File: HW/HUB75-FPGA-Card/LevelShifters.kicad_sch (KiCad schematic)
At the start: 18 parts, among them J11 Conn_01x01, J12 Conn_01x01, J13 Conn_01x01, J14 Conn_01x01, J15 Conn_01x01, J16 Conn_01x01, J2 Conn_01x03, J3 Conn_02x08_Odd_Even, J4 Conn_01x03, J5 Conn_01x03, J6 Conn_02x08_Odd_Even, J7 Conn_01x03, U4 74AHCT245PW, U5 74AHCT245PW, U6 74AHCT245PW

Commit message: saving hardware progress
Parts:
- removed J13, J14, J15, J16: Conn_01x01, Connector_Wire:SolderWirePad_1x01_SMD_1x2mm, symbol Connector_Generic:Conn_01x01
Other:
- note removed: "Aux 5V Pads"
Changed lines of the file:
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@@
-    (effects (font (size 2.54 2.54)) (justify left bottom))
-  )
-  (text "Aux 5V\nPads" (at 255.27 116.84 0)
     (effects (font (size 2.54 2.54)) (justify left bottom))
   )
@@
         (path "/12c1dc17-a9d4-409d-a42e-fc131eeff0fd/eacbd1af-1c38-4bd8-912b-ae623186866b"
           (reference "#PWR048") (unit 1)
-        )
-      )
-    )
-  )
-  (symbol (lib_id "power:+5V") (at 250.19 121.92 0) (unit 1)
-    (in_bom yes) (on_board yes) (dnp no) (fields_autoplaced)
-    (property "Reference" "#PWR0102" (at 250.19 125.73 0)
-      (effects (font (size 1.27 1.27)) hide)
-    )
-    (property "Value" "+5V" (at 250.19 116.84 0)
-      (effects (font (size 1.27 1.27)))
-    )
-    (property "Footprint" "" (at 250.19 121.92 0)
-      (effects (font (size 1.27 1.27)) hide)
-    )
-    (property "Datasheet" "" (at 250.19 121.92 0)
-      (effects (font (size 1.27 1.27)) hide)
-    )
-    (pin "1")
-    (instances
-      (project "HUB75-FPGA-Card"
-        (path "/12c1dc17-a9d4-409d-a42e-fc131eeff0fd/eacbd1af-1c38-4bd8-912b-ae623186866b"
-          (reference "#PWR0102") (unit 1)
         )
       )
@@
         (path "/12c1dc17-a9d4-409d-a42e-fc131eeff0fd/eacbd1af-1c38-4bd8-912b-ae623186866b"
           (reference "J3") (unit 1)
-        )
-      )
-    )
-  )
-  (symbol (lib_id "Connector_Generic:Conn_01x01") (at 255.27 140.97 0) (unit 1)
-    (in_bom yes) (on_board yes) (dnp no) (fields_autoplaced)
-    (property "Reference" "J15" (at 257.81 139.7 0)
-      (effects (font (size 1.27 1.27)) (justify left))
-    )
-    (property "Value" "Conn_01x01" (at 257.81 142.24 0)
-      (effects (font (size 1.27 1.27)) (justify left))
-    )
-    (property "Footprint" "Connector_Wire:SolderWirePad_1x01_SMD_1x2mm" (at 255.27 140.97 0)
-      (effects (font (size 1.27 1.27)) hide)
-    )
-    (property "Datasheet" "~" (at 255.27 140.97 0)
-      (effects (font (size 1.27 1.27)) hide)
-    )
-    (pin "1")
-    (instances
-      (project "HUB75-FPGA-Card"
-        (path "/12c1dc17-a9d4-409d-a42e-fc131eeff0fd/eacbd1af-1c38-4bd8-912b-ae623186866b"
-          (reference "J15") (unit 1)
         )
       )
@@
     )
   )
-  (symbol (lib_id "power:GND") (at 250.19 127 0) (unit 1)
-    (in_bom yes) (on_board yes) (dnp no)
-    (property "Reference" "#PWR0103" (at 250.19 133.35 0)
-      (effects (font (size 1.27 1.27)) hide)
-    )
-    (property "Value" "GND" (at 250.19 130.81 0)
-      (effects (font (size 1.27 1.27)))
-    )
-    (property "Footprint" "" (at 250.19 127 0)
-      (effects (font (size 1.27 1.27)) hide)
-    )
-    (property "Datasheet" "" (at 250.19 127 0)
-      (effects (font (size 1.27 1.27)) hide)
-    )
-    (pin "1")
-    (instances
-      (project "HUB75-FPGA-Card"
-        (path "/12c1dc17-a9d4-409d-a42e-fc131eeff0fd/eacbd1af-1c38-4bd8-912b-ae623186866b"
-          (reference "#PWR0103") (unit 1)
-        )
-      )
-    )
-  )
   (symbol (lib_id "power:GND") (at 106.68 128.27 0) (unit 1)
     (in_bom yes) (on_board yes) (dnp no)
@@
     )
   )
-  (symbol (lib_id "Connector_Generic:Conn_01x01") (at 255.27 146.05 0) (unit 1)
-    (in_bom yes) (on_board yes) (dnp no) (fields_autoplaced)
-    (property "Reference" "J16" (at 257.81 144.78 0)
-      (effects (font (size 1.27 1.27)) (justify left))
-    )
-    (property "Value" "Conn_01x01" (at 257.81 147.32 0)
-      (effects (font (size 1.27 1.27)) (justify left))
-    )
-    (property "Footprint" "Connector_Wire:SolderWirePad_1x01_SMD_1x2mm" (at 255.27 146.05 0)
-      (effects (font (size 1.27 1.27)) hide)
-    )
-    (property "Datasheet" "~" (at 255.27 146.05 0)
-      (effects (font (size 1.27 1.27)) hide)
-    )
-    (pin "1")
-    (instances
-      (project "HUB75-FPGA-Card"
-        (path "/12c1dc17-a9d4-409d-a42e-fc131eeff0fd/eacbd1af-1c38-4bd8-912b-ae623186866b"
-          (reference "J16") (unit 1)
-        )
-      )
-    )
-  )
   (symbol (lib_id "power:+5V") (at 195.58 91.44 0) (unit 1)
     (in_bom yes) (on_board yes) (dnp no) (fields_autoplaced)
@@
         (path "/12c1dc17-a9d4-409d-a42e-fc131eeff0fd/eacbd1af-1c38-4bd8-912b-ae623186866b"
           (reference "J12") (unit 1)
-        )
-      )
-    )
-  )
-  (symbol (lib_id "Connector_Generic:Conn_01x01") (at 255.27 121.92 0) (unit 1)
-    (in_bom yes) (on_board yes) (dnp no) (fields_autoplaced)
-    (property "Reference" "J13" (at 257.81 120.65 0)
-      (effects (font (size 1.27 1.27)) (justify left))
-    )
-    (property "Value" "Conn_01x01" (at 257.81 123.19 0)
-      (effects (font (size 1.27 1.27)) (justify left))
-    )
-    (property "Footprint" "Connector_Wire:SolderWirePad_1x01_SMD_1x2mm" (at 255.27 121.92 0)
-      (effects (font (size 1.27 1.27)) hide)
-    )
-    (property "Datasheet" "~" (at 255.27 121.92 0)
-      (effects (font (size 1.27 1.27)) hide)
-    )
-    (pin "1")
-    (instances
-      (project "HUB75-FPGA-Card"
-        (path "/12c1dc17-a9d4-409d-a42e-fc131eeff0fd/eacbd1af-1c38-4bd8-912b-ae623186866b"
-          (reference "J13") (unit 1)
-        )
-      )
-    )
-  )
-  (symbol (lib_id "Connector_Generic:Conn_01x01") (at 255.27 127 0) (unit 1)
-    (in_bom yes) (on_board yes) (dnp no) (fields_autoplaced)
-    (property "Reference" "J14" (at 257.81 125.73 0)
-      (effects (font (size 1.27 1.27)) (justify left))
-    )
-    (property "Value" "Conn_01x01" (at 257.81 128.27 0)
-      (effects (font (size 1.27 1.27)) (justify left))
-    )
-    (property "Footprint" "Connector_Wire:SolderWirePad_1x01_SMD_1x2mm" (at 255.27 127 0)
-      (effects (font (size 1.27 1.27)) hide)
-    )
-    (property "Datasheet" "~" (at 255.27 127 0)
-      (effects (font (size 1.27 1.27)) hide)
-    )
-    (pin "1")
-    (instances
-      (project "HUB75-FPGA-Card"
-        (path "/12c1dc17-a9d4-409d-a42e-fc131eeff0fd/eacbd1af-1c38-4bd8-912b-ae623186866b"
-          (reference "J14") (unit 1)
         )
       )
@@
     )
   )
-  (symbol (lib_id "power:+5V") (at 250.19 140.97 0) (unit 1)
-    (in_bom yes) (on_board yes) (dnp no) (fields_autoplaced)
-    (property "Reference" "#PWR0104" (at 250.19 144.78 0)
-      (effects (font (size 1.27 1.27)) hide)
-    )
-    (property "Value" "+5V" (at 250.19 135.89 0)
-      (effects (font (size 1.27 1.27)))
-    )
-    (property "Footprint" "" (at 250.19 140.97 0)
-      (effects (font (size 1.27 1.27)) hide)
-    )
-    (property "Datasheet" "" (at 250.19 140.97 0)
-      (effects (font (size 1.27 1.27)) hide)
-    )
-    (pin "1")
-    (instances
-      (project "HUB75-FPGA-Card"
-        (path "/12c1dc17-a9d4-409d-a42e-fc131eeff0fd/eacbd1af-1c38-4bd8-912b-ae623186866b"
-          (reference "#PWR0104") (unit 1)
-        )
-      )
-    )
-  )
   (symbol (lib_id "power:GND") (at 182.88 57.15 0) (unit 1)
     (in_bom yes) (on_board yes) (dnp no)
@@
         )
       )
-    )
-  )
-  (symbol (lib_id "power:GND") (at 250.19 146.05 0) (unit 1)
-    (in_bom yes) (on_board yes) (dnp no)
-    (property "Reference" "#PWR0105" (at 250.19 152.4 0)
-      (effects (font (size 1.27 1.27)) hide)
-    )
-    (property "Value" "GND" (at 250.19 149.86 0)
-      (effects (font (size 1.27 1.27)))
-    )
-    (property "Footprint" "" (at 250.19 146.05 0)
-      (effects (font (size 1.27 1.27)) hide)
-    )
-    (property "Datasheet" "" (at 250.19 146.05 0)
-      (effects (font (size 1.27 1.27)) hide)
-    )
-    (pin "1")
-    (instances
-      (project "HUB75-FPGA-Card"
-        (path "/12c1dc17-a9d4-409d-a42e-fc131eeff0fd/eacbd1af-1c38-4bd8-912b-ae623186866b"
-          (reference "#PWR0105") (unit 1)
-        )
-      )

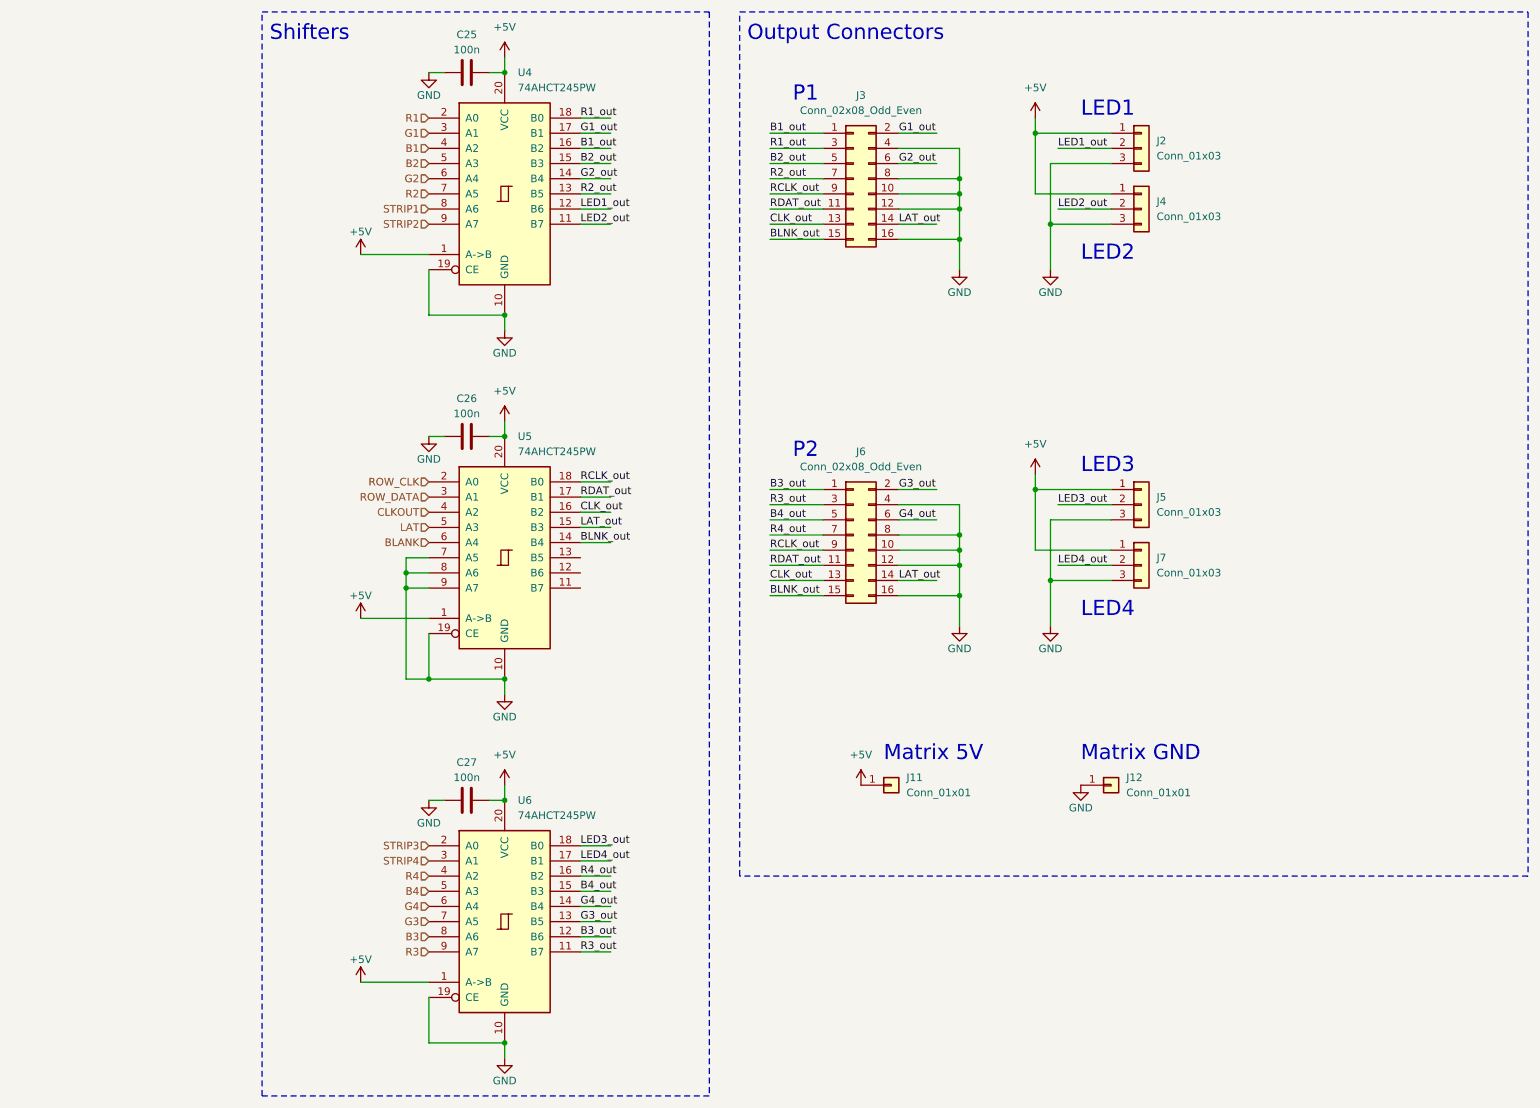
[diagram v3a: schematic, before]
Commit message: initial v1.1 board layout
still needs rp2040 pins routed
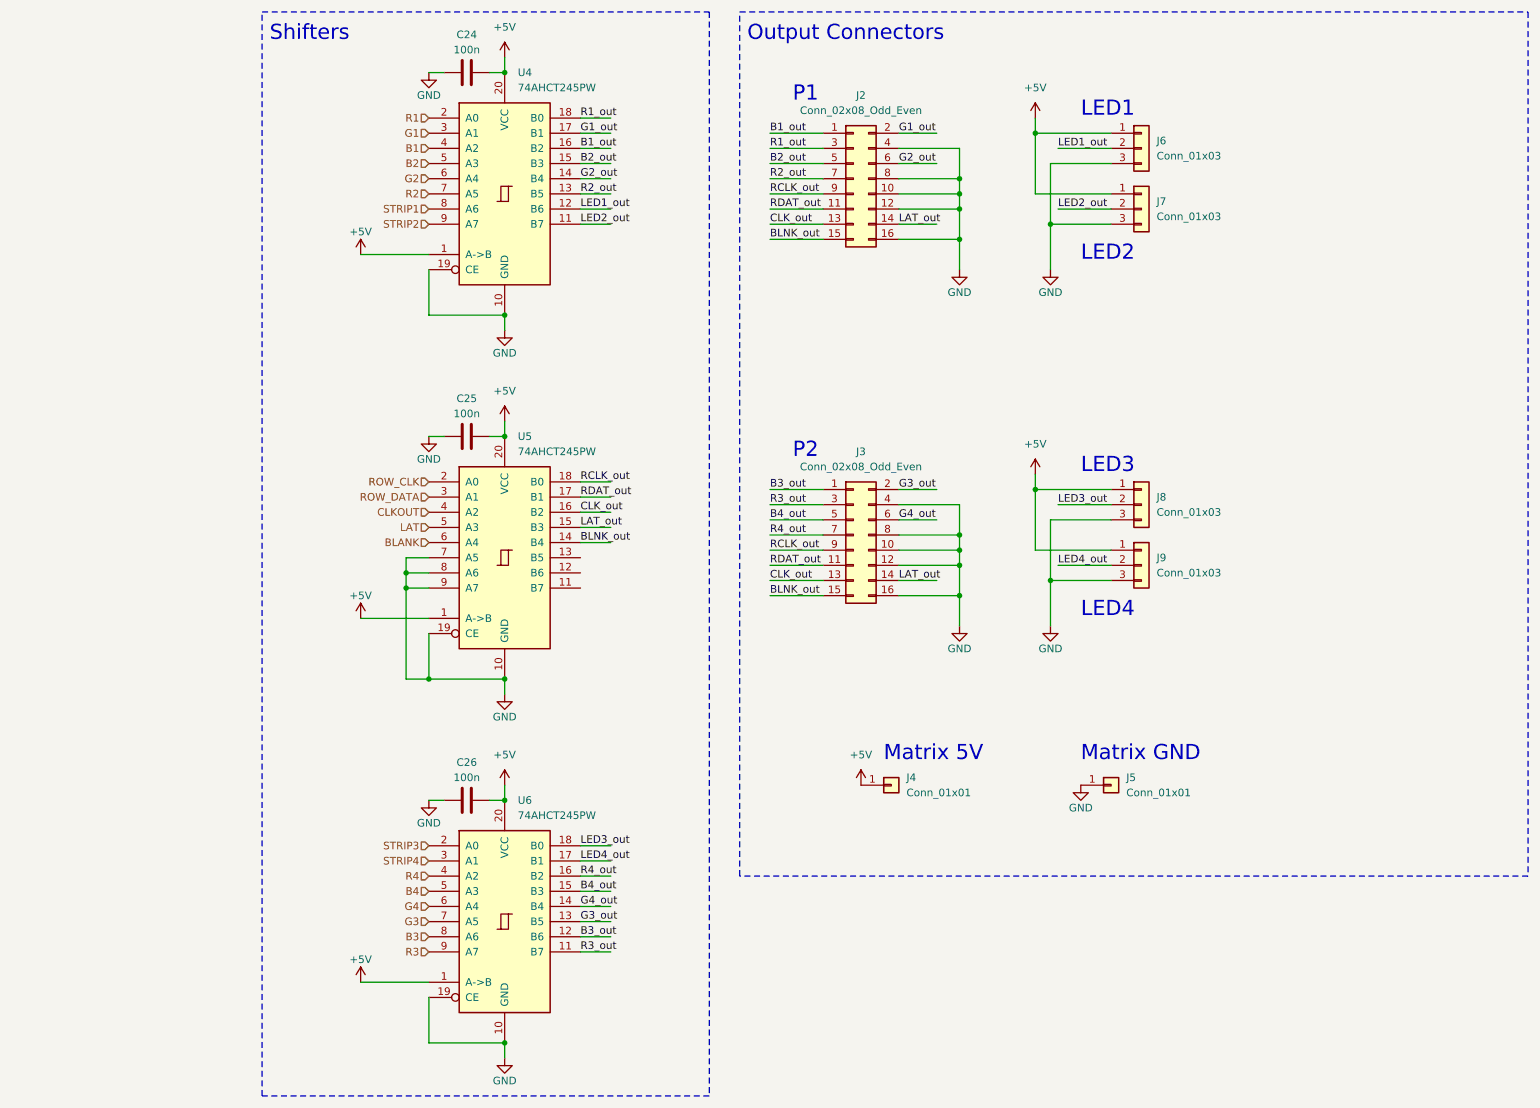
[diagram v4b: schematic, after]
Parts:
- renumbered C25 to C24, C26 to C25, C27 to C26, J3 to J2, J6 to J3, J11 to J4, J12 to J5, J2 to J6, J4 to J7, J5 to J8, J7 to J9

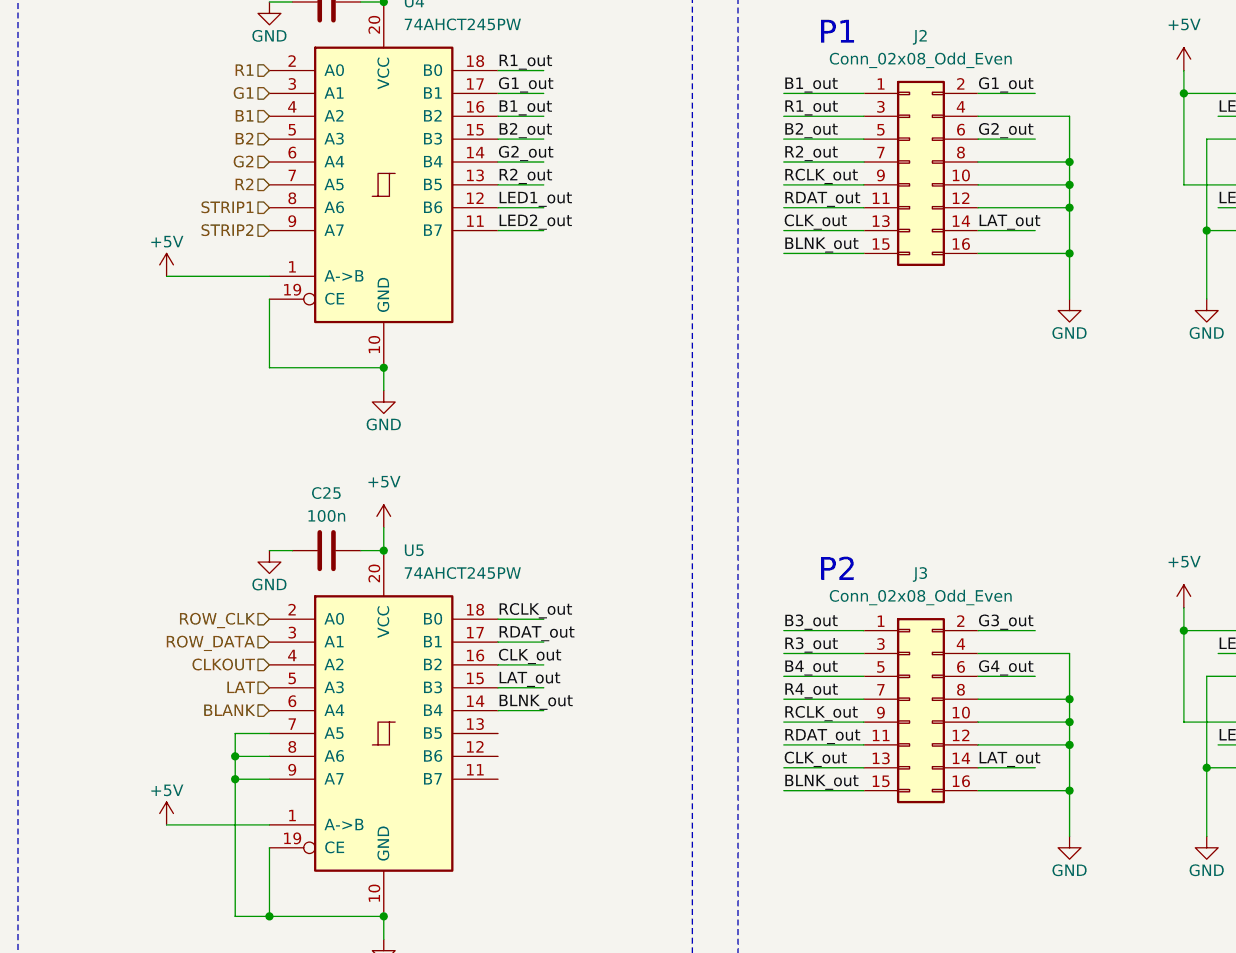
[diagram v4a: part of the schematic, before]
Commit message: update components and generate production files
still need to look into CBSEL
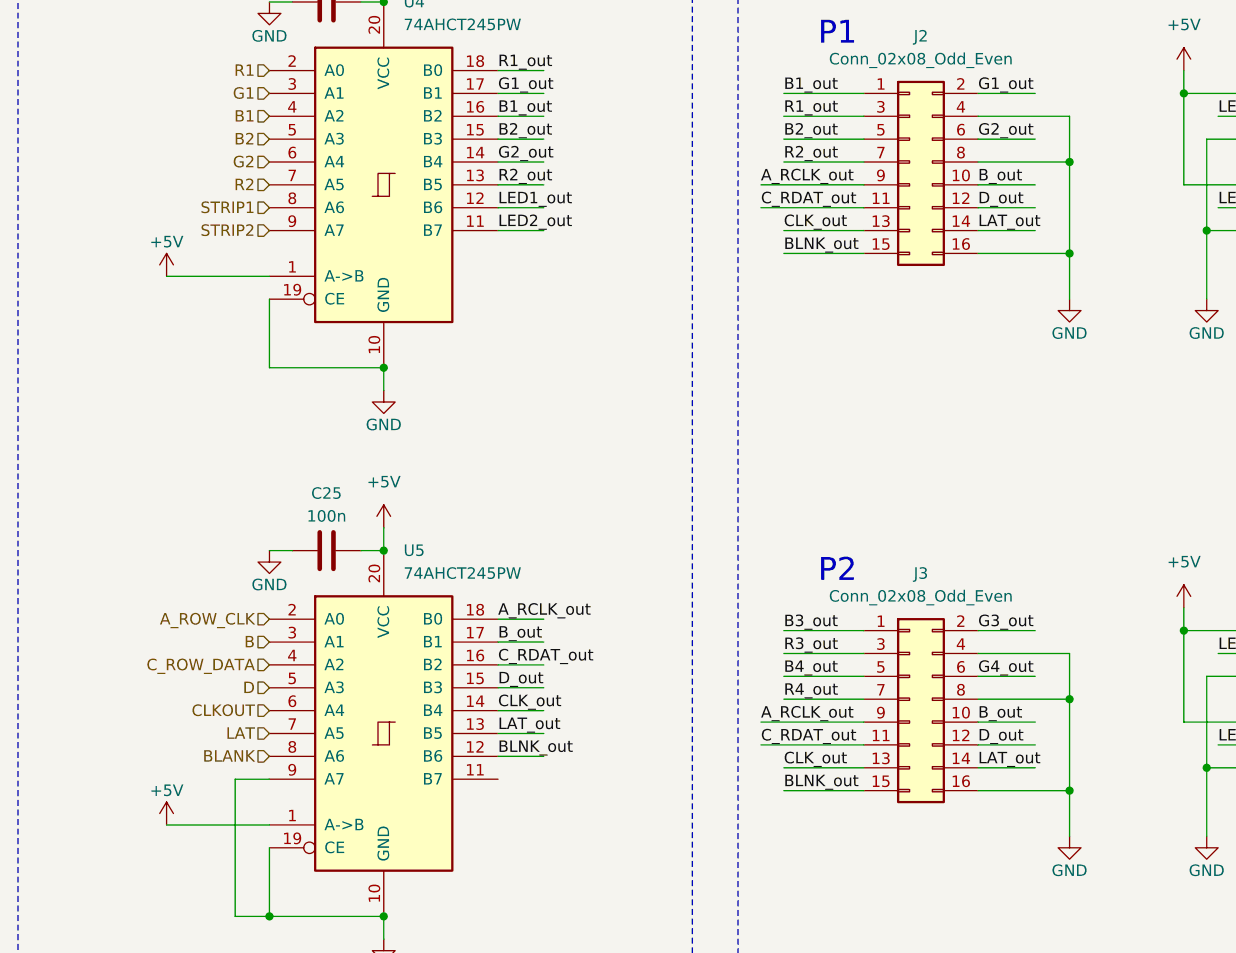
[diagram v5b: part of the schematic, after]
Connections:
- net BLANK: now also U5.8 (A6); no longer U5.6 (A4)
- net BLNK_out: now also U5.12 (B6); no longer U5.14 (B4)
- net CLKOUT: now also U5.6 (A4); no longer U5.4 (A2)
- net CLK_out: now also U5.14 (B4); no longer U5.16 (B2)
- net GND: no longer J2.10 (Pin_10), J2.12 (Pin_12), J3.10 (Pin_10), J3.12 (Pin_12), U5.7 (A5), U5.8 (A6)
- net LAT: now also U5.7 (A5); no longer U5.5 (A3)
- net LAT_out: now also U5.13 (B5); no longer U5.15 (B3)
- net RCLK_out renamed A_RCLK_out
- net RDAT_out renamed C_RDAT_out
- net C_RDAT_out: now also U5.16 (B2); no longer U5.17 (B1)
- net ROW_CLK renamed A_ROW_CLK
- net ROW_DATA renamed B
- new net B_out: J2.10 (Pin_10), J3.10 (Pin_10), U5.17 (B1)
- new net C_ROW_DATA: U5.4 (A2)
- new net D: U5.5 (A3)
- new net D_out: J2.12 (Pin_12), J3.12 (Pin_12), U5.15 (B3)
